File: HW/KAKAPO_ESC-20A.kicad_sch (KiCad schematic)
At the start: 47 parts, among them J1 Pins_2.54_1x3, J2 Pins_2.54_1x3, M1 Mount_M3, M2 Mount_M3, M3 Mount_M3, M4 Mount_M3

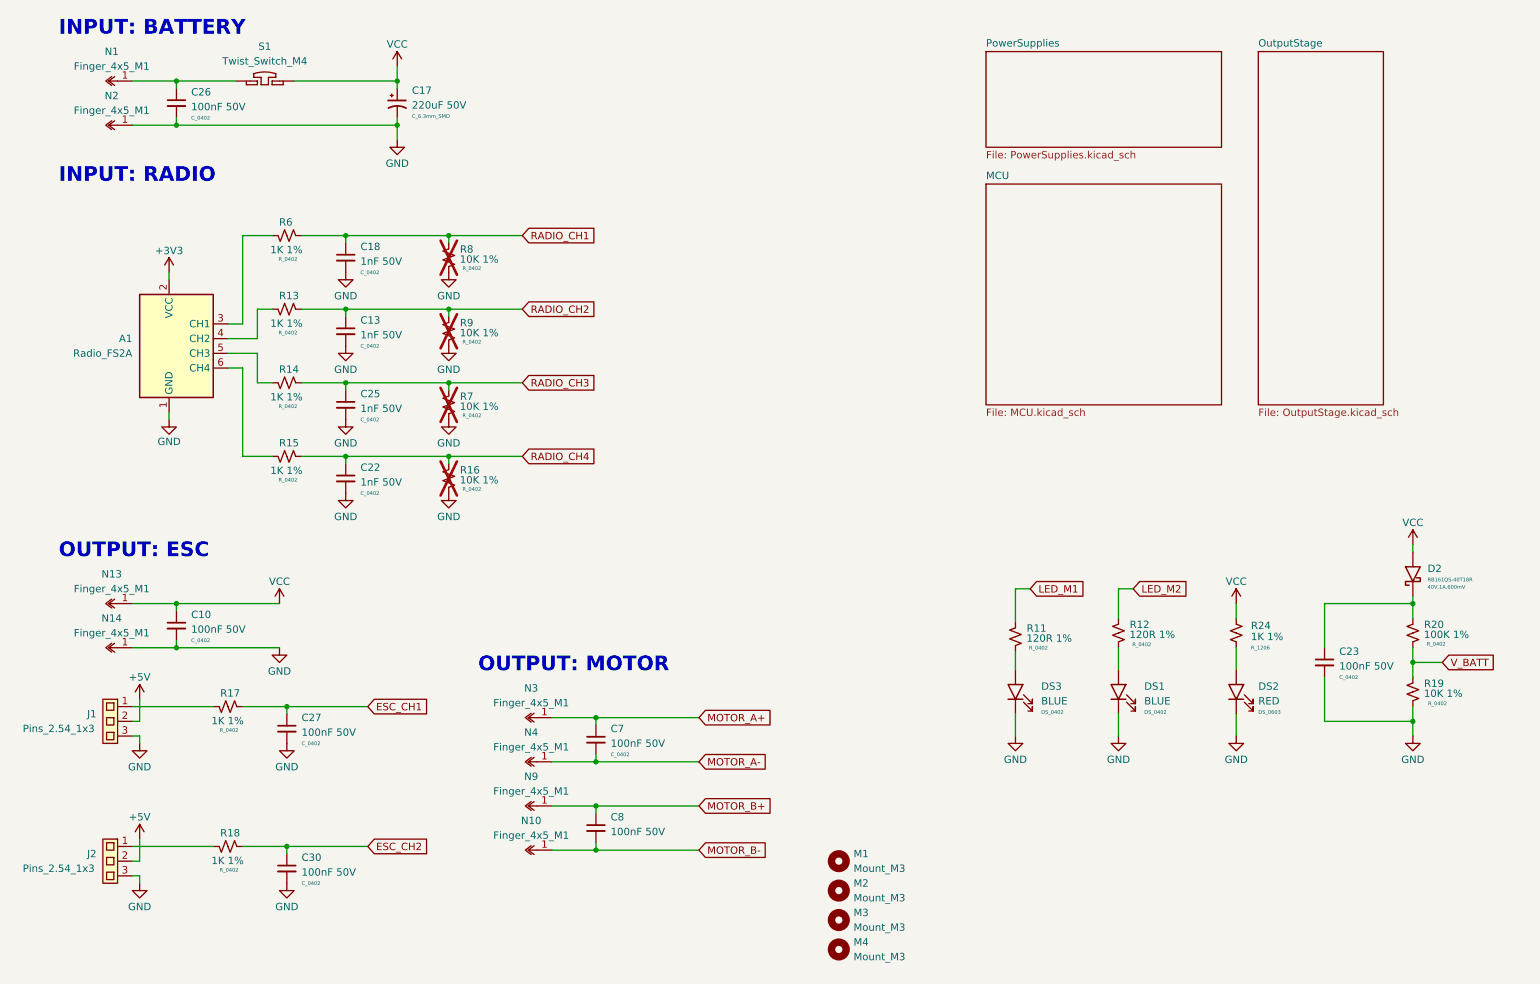
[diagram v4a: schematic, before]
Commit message: Move 5V Supply Around To Make More Efficient Conduction Path
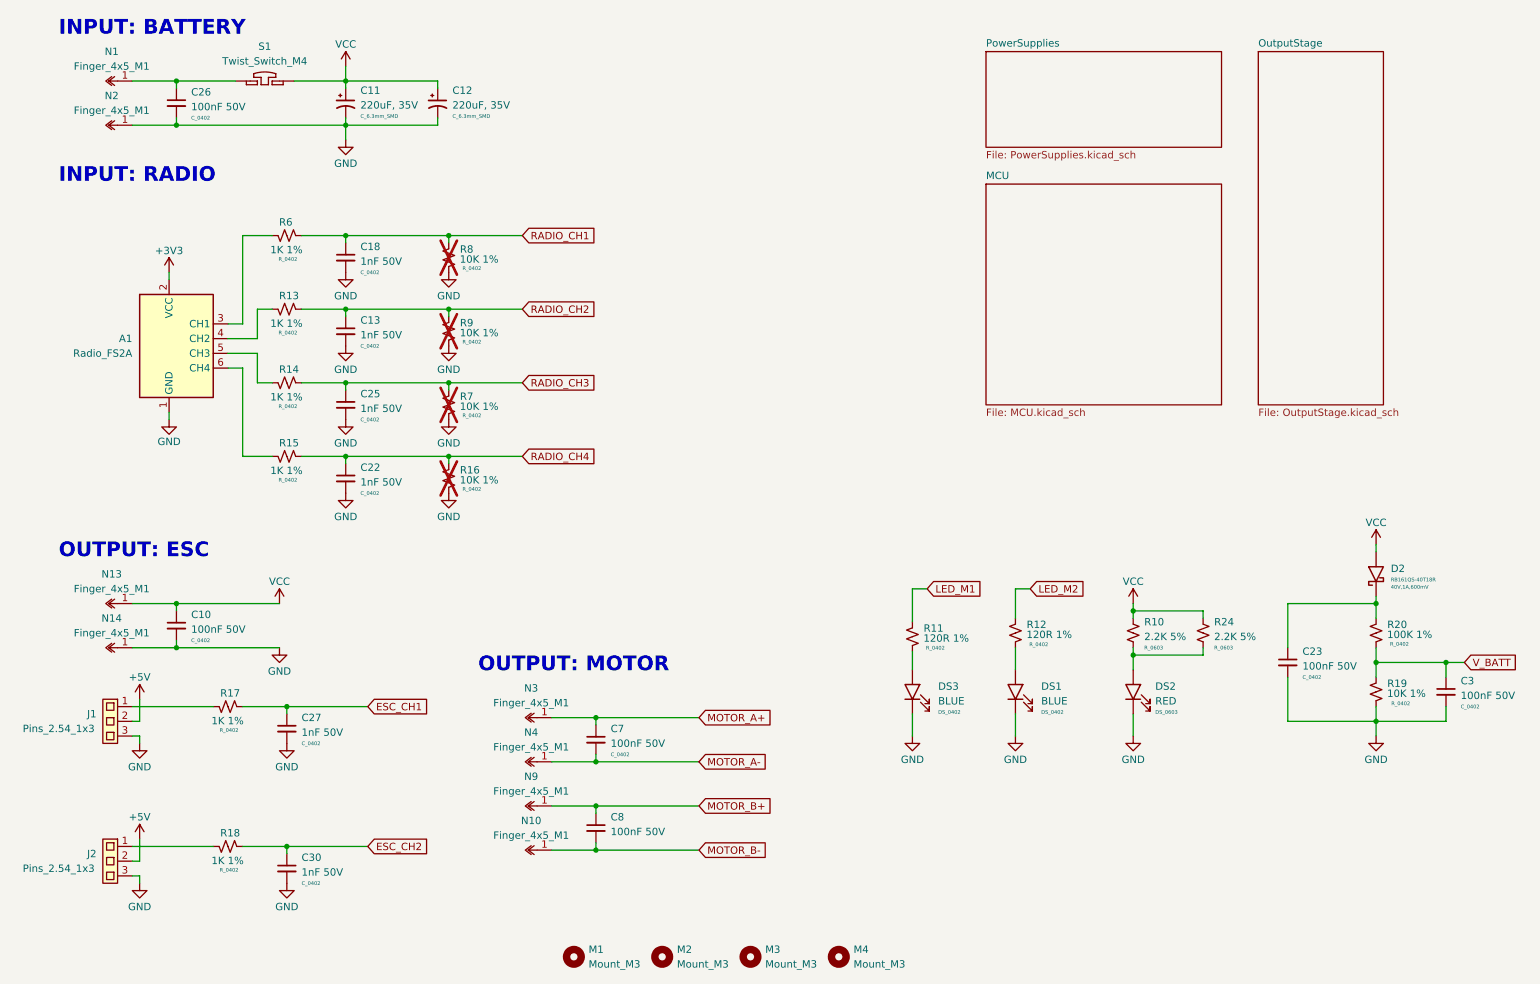
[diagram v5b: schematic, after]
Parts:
- removed C17: 220uF 50V, C_Capacitor:C_6.3mm_SMD, symbol C_Capacitor:C_6.3mm_SMD
- removed R24: 1K 1%, R_Resistor:R_1206, symbol R_Resistor:R_1206
- added C11, C12: 220uF, 35V, C_Capacitor:C_6.3mm_SMD, symbol C_Capacitor:C_6.3mm_SMD
- added C3: 100nF 50V, C_Capacitor:C_0402, symbol C_Capacitor:C_0402
- added R10, R24: 2.2K 5%, R_Resistor:R_0603, symbol R_Resistor:R_0603
- C13, C18, C22, C25: LCSC Part C105882 -> C106205
- C27, C30: value 100nF 50V -> 1nF 50V; LCSC Part C105882 -> C106205
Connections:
- net GND: now also C11.2, C12.2, C3.2
- net VCC: now also C11.1, C12.1, R10.1, R24.1
- net V_BATT: now also C3.1
- net at DS2.2 (A): now also R10.2, R24.2
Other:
- moved on the sheet: C23, D2, DS1, DS2, DS3, M1, M2, M3, M4, R11, R12, R19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
